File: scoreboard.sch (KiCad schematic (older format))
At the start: 77 parts

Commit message: Prepare for first order
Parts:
- removed C?: 1uF, symbol C
- removed D?: D, symbol D
- removed J?: UART, symbol CONN_01X03
- added C103: 1uF, Capacitors_SMD:C_0603_HandSoldering, symbol C
- added LOGO101, LOGO102, LOGO103: OPEN_HARDWARE_1, Symbols:Symbol_OSHW-Logo_CopperTop, symbol OPEN_HARDWARE_1
- added Q110: FDN340P, TO_SOT_Packages_SMD:SOT-23_Handsoldering, symbol Q_PMOS_GSD
- ADDR1, ADDR2, ADDR3: footprint (none) -> solder_jumper:solder_jumper
- C101, C102, C104, C105: renamed from C?; footprint (none) -> Capacitors_SMD:C_0603_HandSoldering
- D102: renamed from D?; footprint (none) -> led_0603_handsoldering:led_0603_HandSoldering
- D103, D104, D105, D106, D107, D108, D109, D110, D111, D112, D113, D114, D115, D116, D117, D118, D119, D120: renamed from D?; footprint (none) -> LEDs:LED_D5.0mm
- J101, J105, J106, J107, J108, J109, J110, J111, J112, J113: renamed from J?; footprint (none) -> Connect:AK300-min
- J102: renamed from J?; footprint (none) -> Connectors_Molex:Molex_MicroLatch-53253-0370_03x2.00mm_Straight
- J104: renamed from J?; footprint (none) -> Connect:Tag-Connect_TC2030-IDC-FP
- JP101, JP102: renamed from JP?; footprint (none) -> Resistors_SMD:R_0603_HandSoldering
- R101, R102, R103, R104, R105, R106, R107, R111, R112, R113, R116, R118, R119, R122: renamed from R?; footprint (none) -> Resistors_SMD:R_0603_HandSoldering
- R108, R109, R110, R114, R115, R117, R120, R121, R123: renamed from R?; footprint (none) -> Resistors_ThroughHole:R_Axial_DIN0411_L9.9mm_D3.6mm_P15.24mm_Horizontal
- U101: renamed from U?; footprint (none) -> TO_SOT_Packages_SMD:SOT-23_Handsoldering
- U102: renamed from U?; footprint (none) -> soic-14w:SOIC-14W_7.5x10.3mm_Pitch1.27mm
- gave numbers to parts that had none: 9
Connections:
- net +6V: now also C103.1, Q110.2 (S)
- net GND: now also C103.2, Q110.1 (G)
- net SWCLK: now also Q104.1 (G), R106.2, R107.1; no longer Q103.1 (G), R105.1
- net TX: no longer R119.2
- net at Q105.1 (G), R111.1, U102.13 (PA02): now also ADDR1.1; no longer ADDR1.2
- net at J101.2 (P2): now also Q110.3 (D)
- net at R106.1: now also ADDR1.2; no longer ADDR1.1
- new net: Q103.1 (G), R105.1, R119.2, U102.10 (PA25)
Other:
- note added: "Approx 0.5A\n(20mA per string * 3 * 7 segments)"
- note added: "Place near C105"
- note removed: "DNF"
- moved on the sheet: ADDR1, ADDR2, ADDR3, C101, C104, C105, D102, J101, J104, J105, J107, J108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

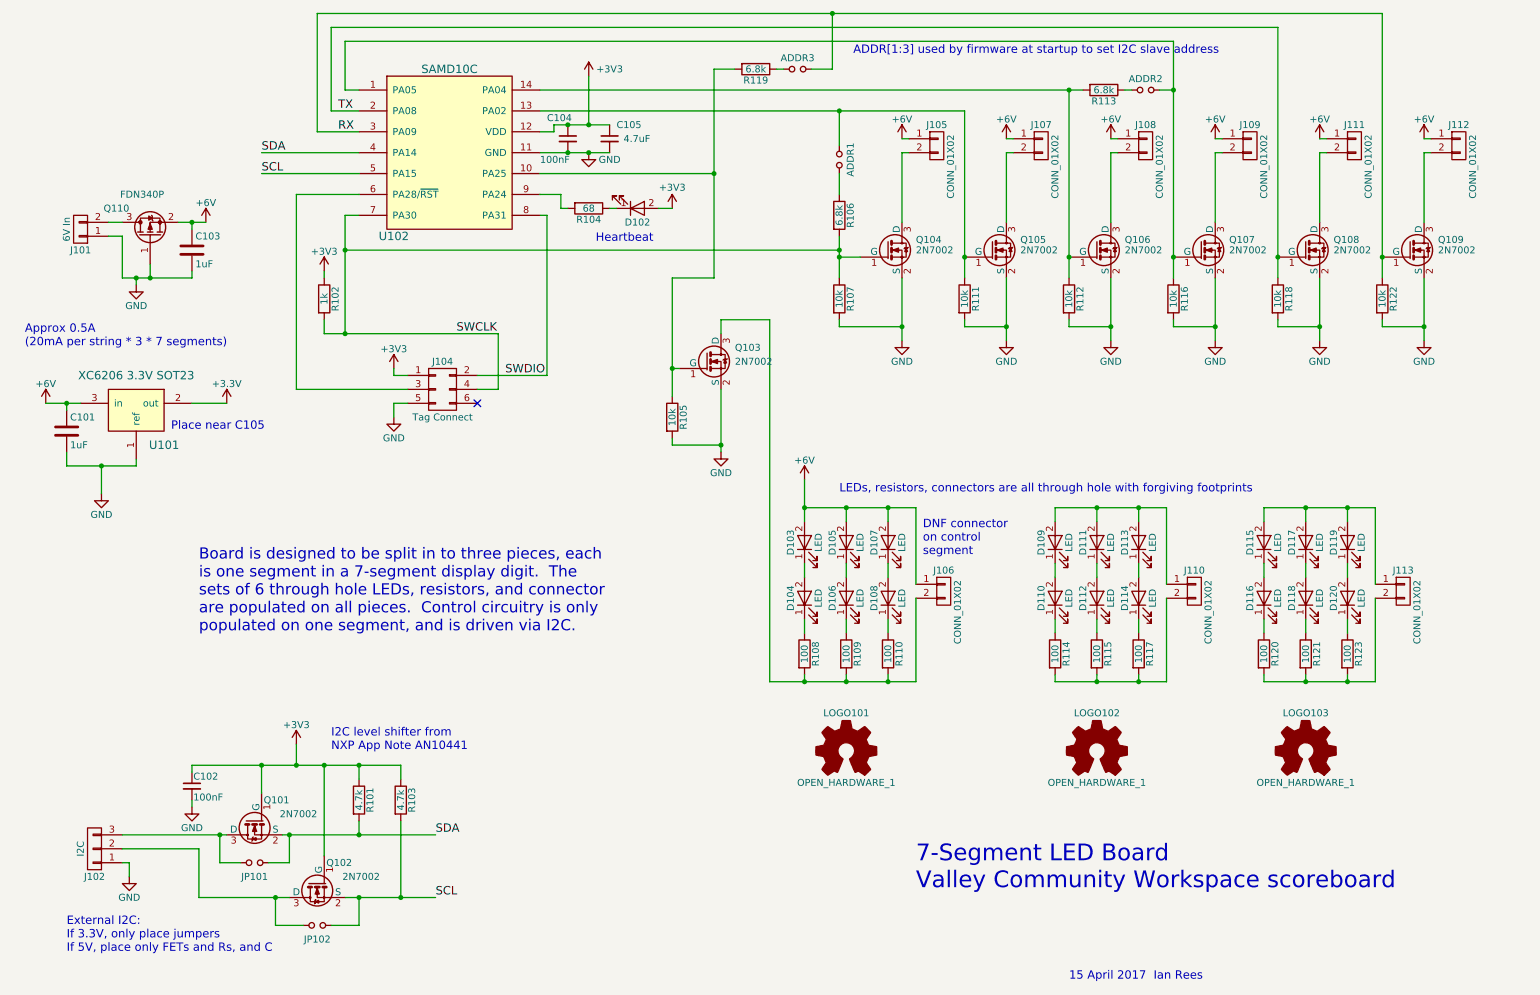
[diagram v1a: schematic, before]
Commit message: PCB updated and gerbers added as ordered
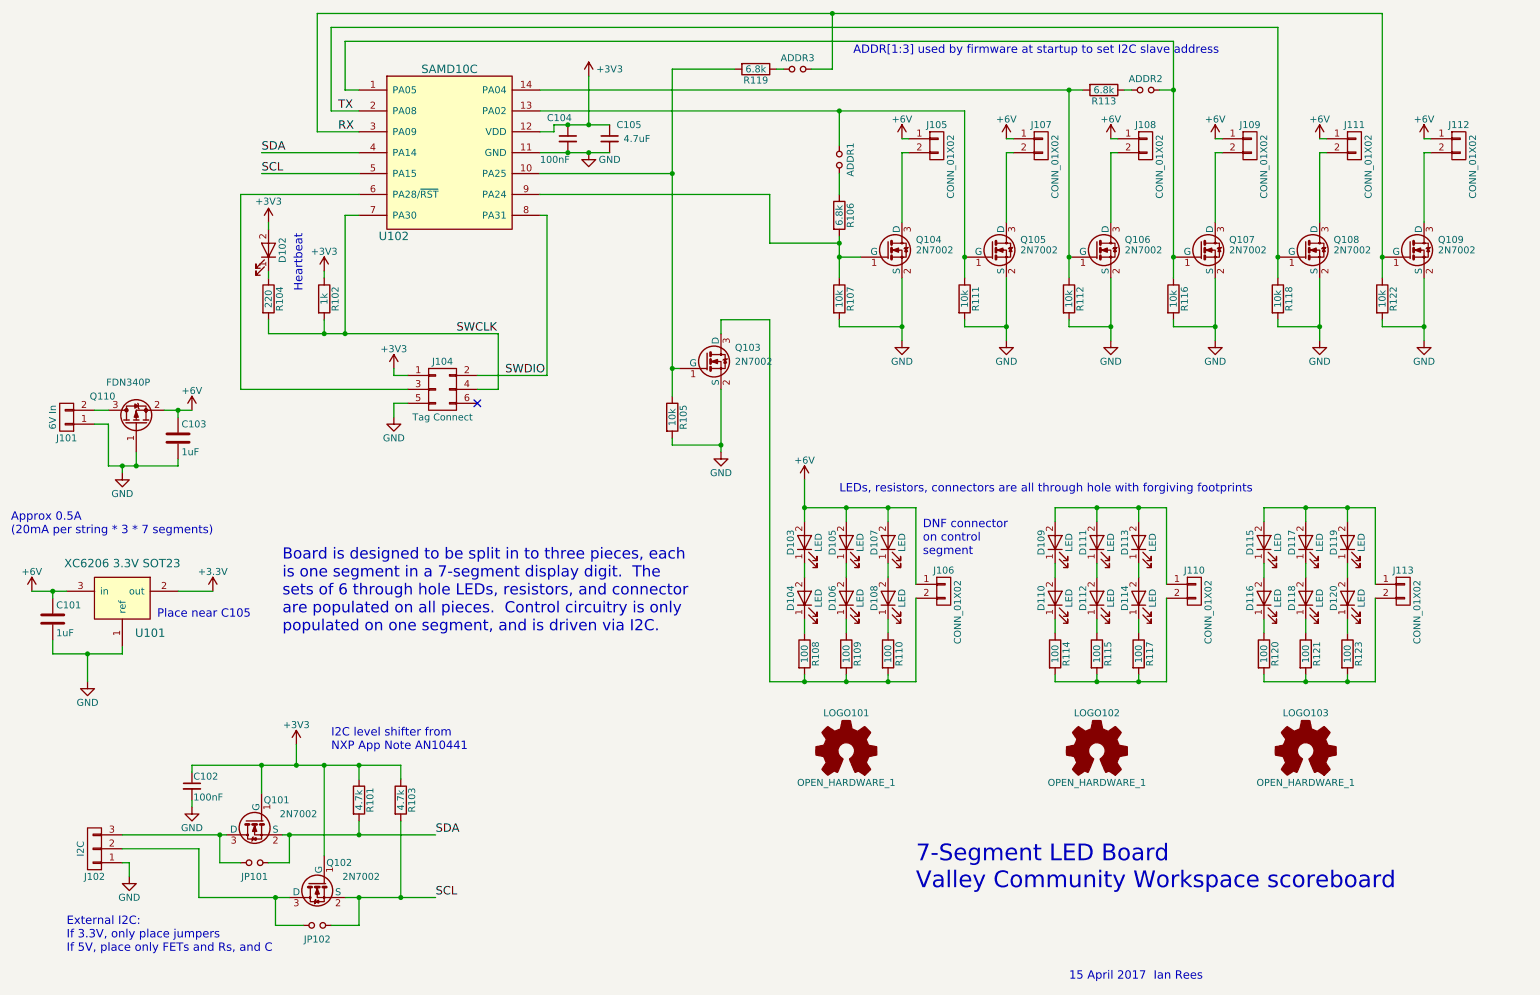
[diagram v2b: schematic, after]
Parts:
- R104: value 68 -> 220
- U102: footprint soic-14w:SOIC-14W_7.5x10.3mm_Pitch1.27mm -> Housings_SOIC:SOIC-14_3.9x8.7mm_Pitch1.27mm
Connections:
- net SWCLK: now also R104.2; no longer Q104.1 (G), R106.2, R107.1
- net at U102.9 (PA24): now also Q104.1 (G), R106.2, R107.1; no longer R104.2
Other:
- moved on the sheet: C101, C103, D102, J101, Q110, R104, U101
